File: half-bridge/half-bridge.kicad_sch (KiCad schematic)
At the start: 50 parts, among them J1 Conn_01x11_Pin, J2 Conn_01x11_Pin, J3 Conn_01x04_Pin, J4 Conn_01x04_Pin, J5 Conn_01x11_Pin, J6 Conn_01x11_Pin, J7 Conn_01x11_Pin, J8 Conn_01x11_Pin, Q1 GAN7R0-150LBE, Q2 GAN7R0-150LBE, U1 LMG1210

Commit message: More work mainly on layout
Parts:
- removed C1: C, Capacitor_SMD:C_1206_3216Metric, symbol Device:C
- added C1, C2: C_Small, Capacitor_SMD:C_0603_1608Metric, symbol Device:C_Small
- added FL1, FL2: Filter_EMI_CommonMode, symbol Device:Filter_EMI_CommonMode
- renumbered C9 to C10, C10 to C11, C2 to C3, C3 to C4, C4 to C5, C5 to C6, C6 to C7, C7 to C8, C8 to C9
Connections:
- net +5V: now also U1.5 (DHL)
- net Earth: now also FL1.3, FL2.3
- net GNDPWR: now also C1.2, C2.2, FL1.4, FL2.4
- net at J2.1 (Pin_1): now also FL1.1
- net at J2.2 (Pin_2): now also FL2.1
- net POWER_LOW: now reaches C21.1, C22.1, C23.1, C24.1, C25.1, C26.1, C27.1, C28.1, C29.1, C30.1, J3.1 (Pin_1), J5.10 (Pin_10), J5.2 (Pin_2), J5.4 (Pin_4), J5.6 (Pin_6), J5.8 (Pin_8), J6.10 (Pin_10), J6.2 (Pin_2), J6.4 (Pin_4), J6.6 (Pin_6), J6.8 (Pin_8), R11.1
- net POWER_LOW: now also FL1.2
- net Vbus renamed POWER_HIGH
- net POWER_HIGH: now also C1.1, C2.1, FL2.2
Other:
- note added: "Feedback"
- note added: "curret sense"
- moved on the sheet: C10, C11, C3, C4, C5, C6, C7, C8, C9, J7, J8

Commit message: Some changes
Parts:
- added C12, C13: ?pF, Capacitor_SMD:C_0402_1005Metric_Pad0.74x0.62mm_HandSolder, symbol Device:C_Small
- added C95: YFF18PW0J474M, Library:C_0603_1608Metric_Feedthrough_W_Vias, symbol Device:C_Feedthrough
- added C96: 10uF, Capacitor_SMD:C_0603_1608Metric, symbol Device:C_Small
- added R14, R15: 100R, Capacitor_SMD:C_0603_1608Metric, symbol Device:R_Small
- C98, C99: footprint Library:C_0603_1608Metric_Feedthrough -> Library:C_0603_1608Metric_Feedthrough_W_Vias
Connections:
- net +5V: now also C95.1; no longer C98.1, C98.3, U1.4 (Vdd)
- net Earth: now also C12.2, C13.2, C95.2, C96.2
- net at R10.2, R2.2, R4.2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: now also R15.1; no longer U1.19 (PWM/LO)
- net at R1.2, R3.2, R5.2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: now also R14.1; no longer U1.18 (EN/HI)
- new net: C13.1, R15.2, U1.19 (PWM/LO)
- new net: C12.1, R14.2, U1.18 (EN/HI)
- new net: C95.3, C96.1, C98.1, C98.3, U1.4 (Vdd)
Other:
- note added: "TODO: * Filter på insignal? * Filter på kraft IN och/eller UT? * Kylning? * Mer snabb capp över IN? Ä Strömmät INA310A-Q1"
- note removed: "TODO: * Filter på insignal? * Filter på kraft IN och/eller UT? * Kylning? * Mer snabb capp över IN?"
- moved on the sheet: FL1, FL2, J2

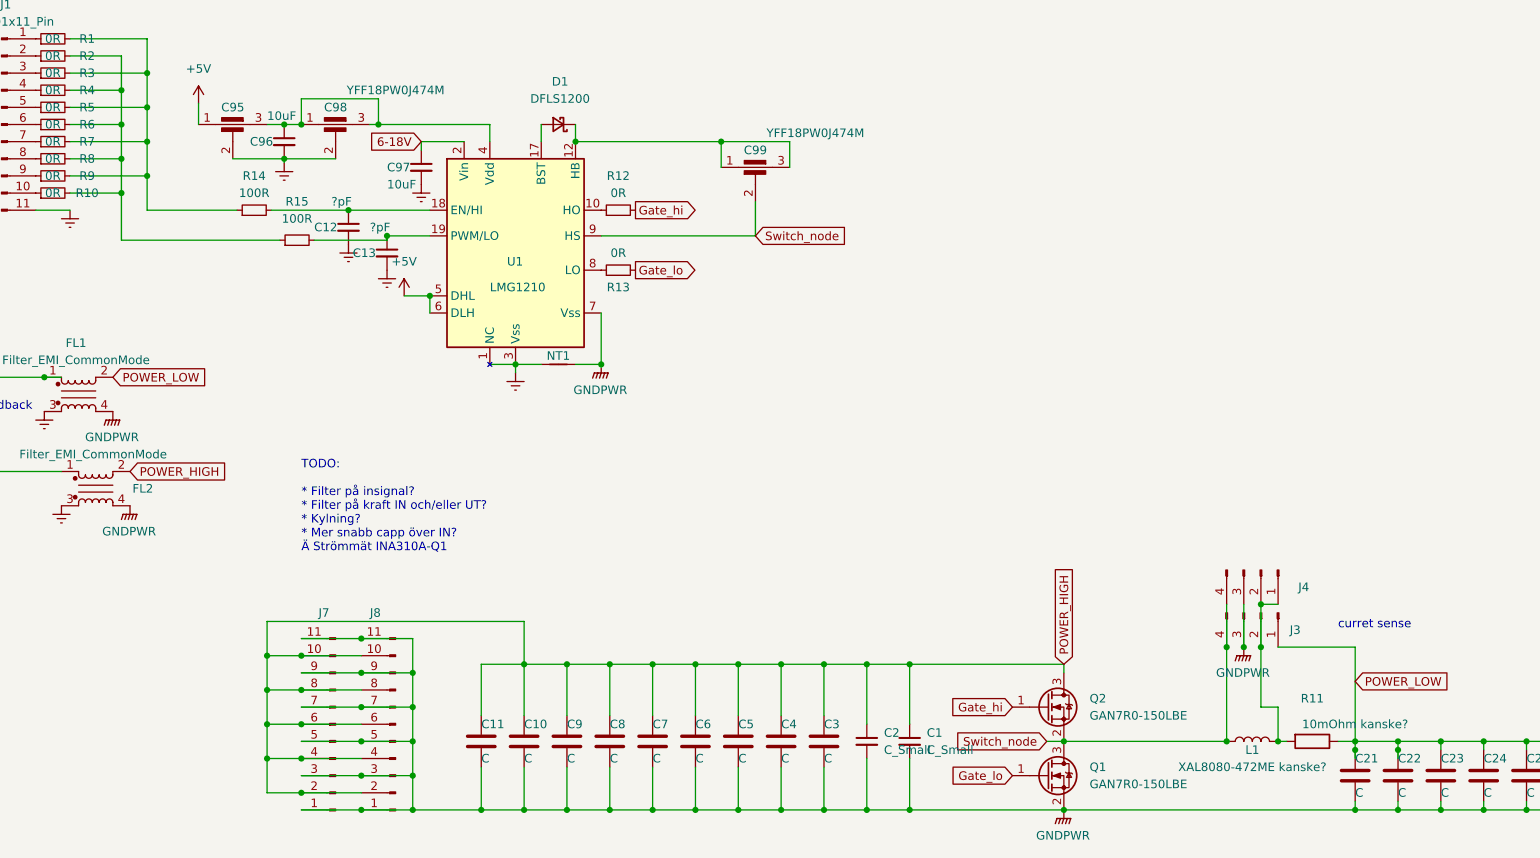
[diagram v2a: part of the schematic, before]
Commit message: Start adding inductor current sense, adjust some vias and add input filtering
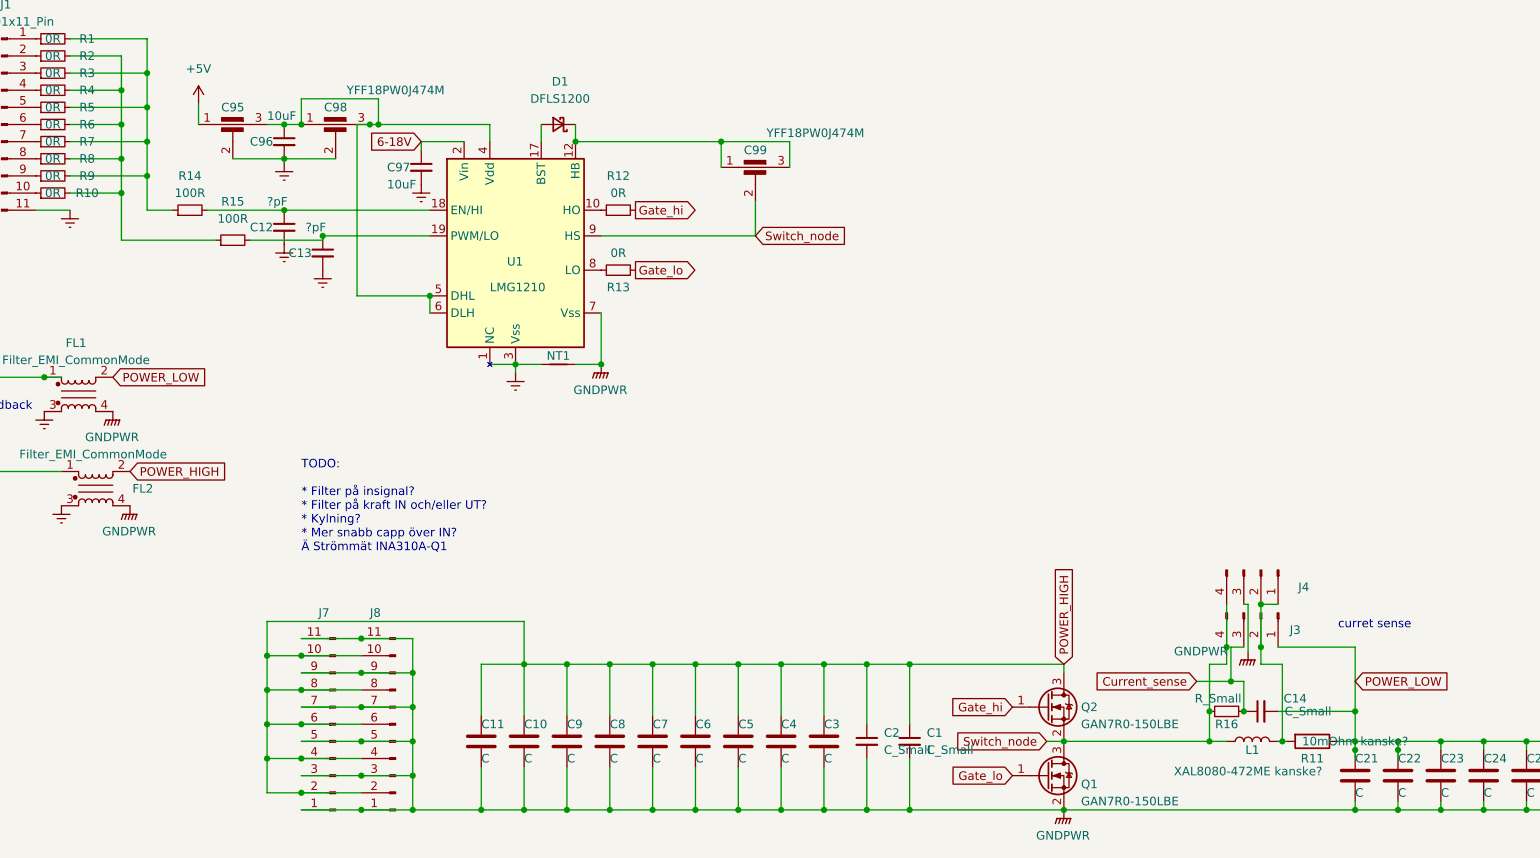
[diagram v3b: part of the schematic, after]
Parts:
- added C14: C_Small, Resistor_SMD:R_0603_1608Metric, symbol Device:C_Small
- added R16: R_Small, Resistor_SMD:R_1206_3216Metric, symbol Device:R_Small
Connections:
- net +5V: no longer U1.5 (DHL), U1.6 (DLH)
- net GNDPWR: no longer J3.3 (Pin_3)
- net POWER_LOW: now also C14.2
- net Switch_node: now also R16.1
- net at C95.3, C96.1, C98.1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: now also U1.5 (DHL), U1.6 (DLH)
- new net Current_sense: C14.1, J3.3 (Pin_3), R16.2
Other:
- moved on the sheet: C12, C13, R14, R15

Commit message: More work on current sense
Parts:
- removed R11: 10mOhm kanske?, Resistor_SMD:R_2816_7142Metric, symbol Device:R
- added NT2: NetTie_2, NetTie:NetTie-2_SMD_Pad0.5mm, symbol Device:NetTie_2
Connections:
- net GNDPWR: now also J3.3 (Pin_3)
- net POWER_LOW: now also J4.1 (Pin_1), L1.2, NT2.2
- net Current_sense renamed Current_sense+
- net Current_sense+: now also J3.2 (Pin_2); no longer J3.3 (Pin_3)
- new net Current_sense-: J4.2 (Pin_2), NT2.1
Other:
- note added: "TODO: * Filter på insignal? * Filter på kraft IN och/eller UT? * Kylning? * Mer snabb capp över IN? * Strömmät INA310A-Q1? * Alternativt, mät ström m.h.a. loss less inductor current measurement https://www.microsemi.com/document-portal/doc_view/14646-an-7-a-simple-current-sense-technique-eliminating-a-sense-resistor"
- note removed: "TODO: * Filter på insignal? * Filter på kraft IN och/eller UT? * Kylning? * Mer snabb capp över IN? Ä Strömmät INA310A-Q1"
- moved on the sheet: C14, J3, J4, R16

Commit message: More work on layout
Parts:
- removed J3, J4: Conn_01x04_Pin, Connector_PinHeader_2.54mm:PinHeader_1x04_P2.54mm_Vertical, symbol Connector:Conn_01x04_Pin
- added C31, C32, C33, C34: C, Capacitor_SMD:C_1210_3225Metric, symbol Device:C
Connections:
- net Current_sense-: now also C14.2
- net GNDPWR: now also C31.2, C32.2, C33.2, C34.2
- net POWER_LOW: now also C31.1, C32.1, C33.1, C34.1; no longer C14.2
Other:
- moved on the sheet: J5, J6, NT2

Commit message: More work on layout
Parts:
- added HS1, HS2, HS3: Heatsink_Pad, Library:Heatsink_SMD_Chamfered_5.2x5.2mm, symbol Mechanical:Heatsink_Pad
- C21, C22, C23, C24, C25, C26, C27, C28: value C -> 220nF
- C29, C30: value C -> 330nF; footprint Capacitor_SMD:C_1206_3216Metric -> Capacitor_SMD:C_1210_3225Metric
- C31, C32, C33, C34: value C -> 330nF
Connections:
- net GNDPWR: now also HS2.1
- net POWER_HIGH: now also HS1.1
- net POWER_LOW: now also HS3.1
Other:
- note added: "1.75uF"
- note added: "2uF"
- moved on the sheet: C29, C30

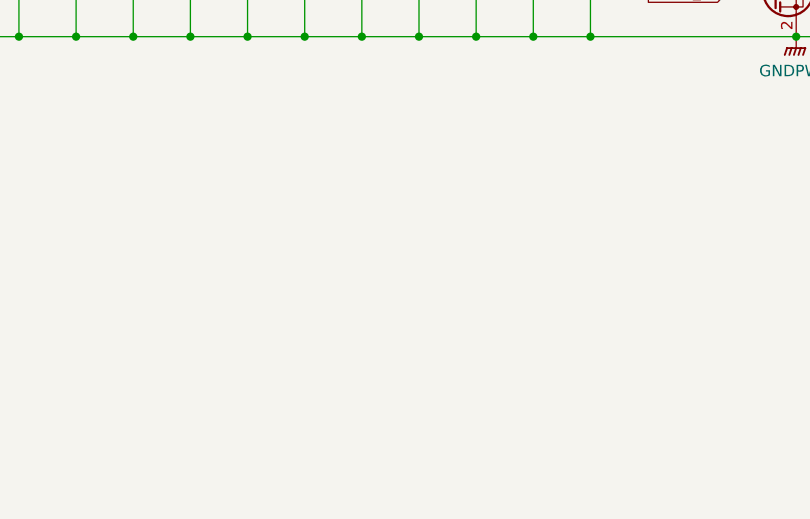
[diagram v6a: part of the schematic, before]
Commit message: More work on layout for current signals
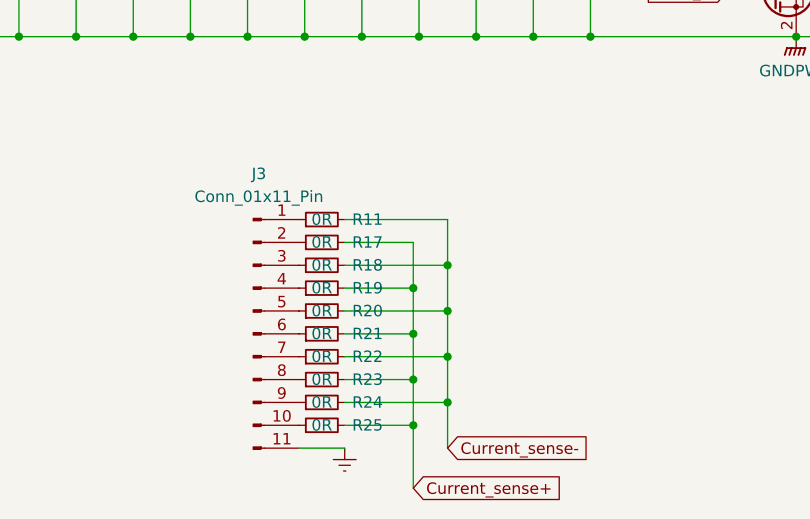
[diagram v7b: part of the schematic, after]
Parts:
- added J3: Conn_01x11_Pin, Connector_PinHeader_2.54mm:PinHeader_1x11_P2.54mm_Vertical, symbol Connector:Conn_01x11_Pin
- added R11, R17, R18, R19, R20, R21, R22, R23, R24, R25: 0R, Capacitor_SMD:C_0402_1005Metric_Pad0.74x0.62mm_HandSolder, symbol Device:R_Small
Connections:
- net Current_sense+: now also R17.2, R19.2, R21.2, R23.2, R25.2
- net Current_sense-: now also R11.2, R18.2, R20.2, R22.2, R24.2
- net Earth: now also J3.11 (Pin_11)
- new net: J3.1 (Pin_1), R11.1
- new net: J3.7 (Pin_7), R22.1
- new net: J3.10 (Pin_10), R25.1
- new net: J3.2 (Pin_2), R17.1
- new net: J3.3 (Pin_3), R18.1
- new net: J3.4 (Pin_4), R19.1
- new net: J3.5 (Pin_5), R20.1
- new net: J3.6 (Pin_6), R21.1
- new net: J3.8 (Pin_8), R23.1
- new net: J3.9 (Pin_9), R24.1

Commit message: More cap
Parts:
- added C12, C13, C14, C15, C16, C17, C18, C19, C35, C36, C37, C38, C39, C40: 330nF, Capacitor_SMD:C_1210_3225Metric, symbol Device:C
- C10, C11: value C -> 330nF; footprint Capacitor_SMD:C_1206_3216Metric -> Capacitor_SMD:C_1210_3225Metric
- C21, C22: value 220nF -> 330nF; footprint Capacitor_SMD:C_1206_3216Metric -> Capacitor_SMD:C_1210_3225Metric
- C3, C4, C5, C6, C7, C8, C9: value C -> 220nF
- renumbered C14 to C92, C13 to C93, C12 to C94
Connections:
- net GNDPWR: now also C12.2, C13.2, C14.2, C15.2, C16.2, C17.2, C18.2, C19.2, C35.2, C36.2, C37.2, C38.2, C39.2, C40.2
- net POWER_HIGH: now also C12.1, C13.1, C14.1, C15.1, C16.1, C17.1, C18.1, C19.1
- net POWER_LOW: now also C35.1, C36.1, C37.1, C38.1, C39.1, C40.1
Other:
- note added: "1.3uF"
- note added: "1.5uF"
- note added: "3.3uF"
- note added: "4.6uF"
- note removed: "1.75uF"
- note removed: "2uF"
- moved on the sheet: C10, C11, C21, C22, C23, C24, C25, C26, C27, C28, C29, C30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
